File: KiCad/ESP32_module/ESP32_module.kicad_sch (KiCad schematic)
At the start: 35 parts, among them J1 Conn_01x05_Pin, J2 Conn_01x05_Pin, J3 Conn_01x05_Pin, J4 Conn_01x05_Pin, J5 Conn_01x02_Pin, J6 Conn_01x02_Pin, J7 Conn_01x02_Pin, J8 Conn_01x02_Pin, J9 Conn_01x02_Pin, M1 ESP32_XAIO

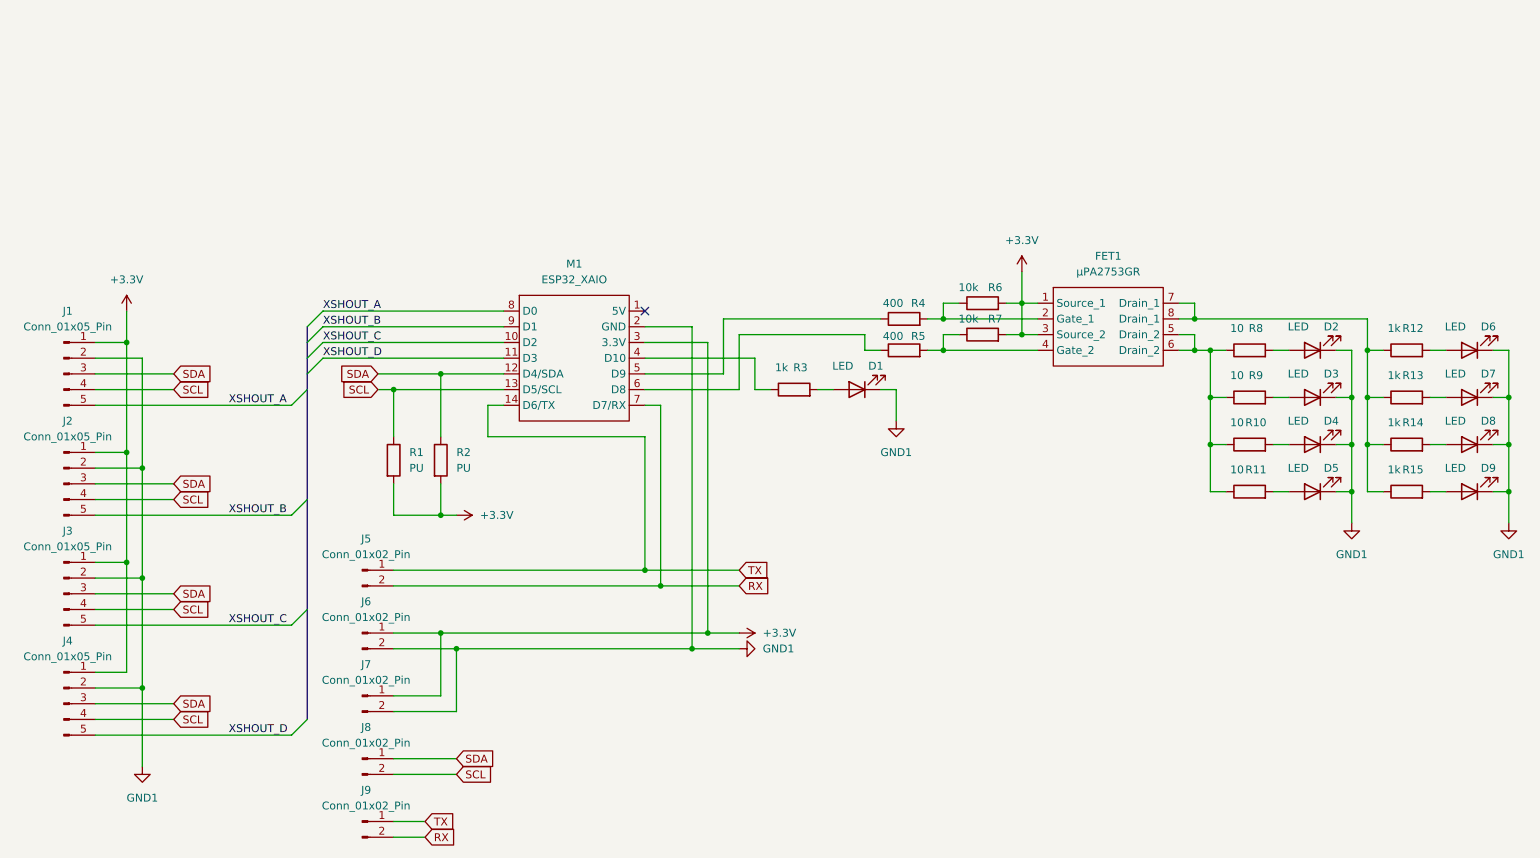
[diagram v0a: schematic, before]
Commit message: fix mosfet
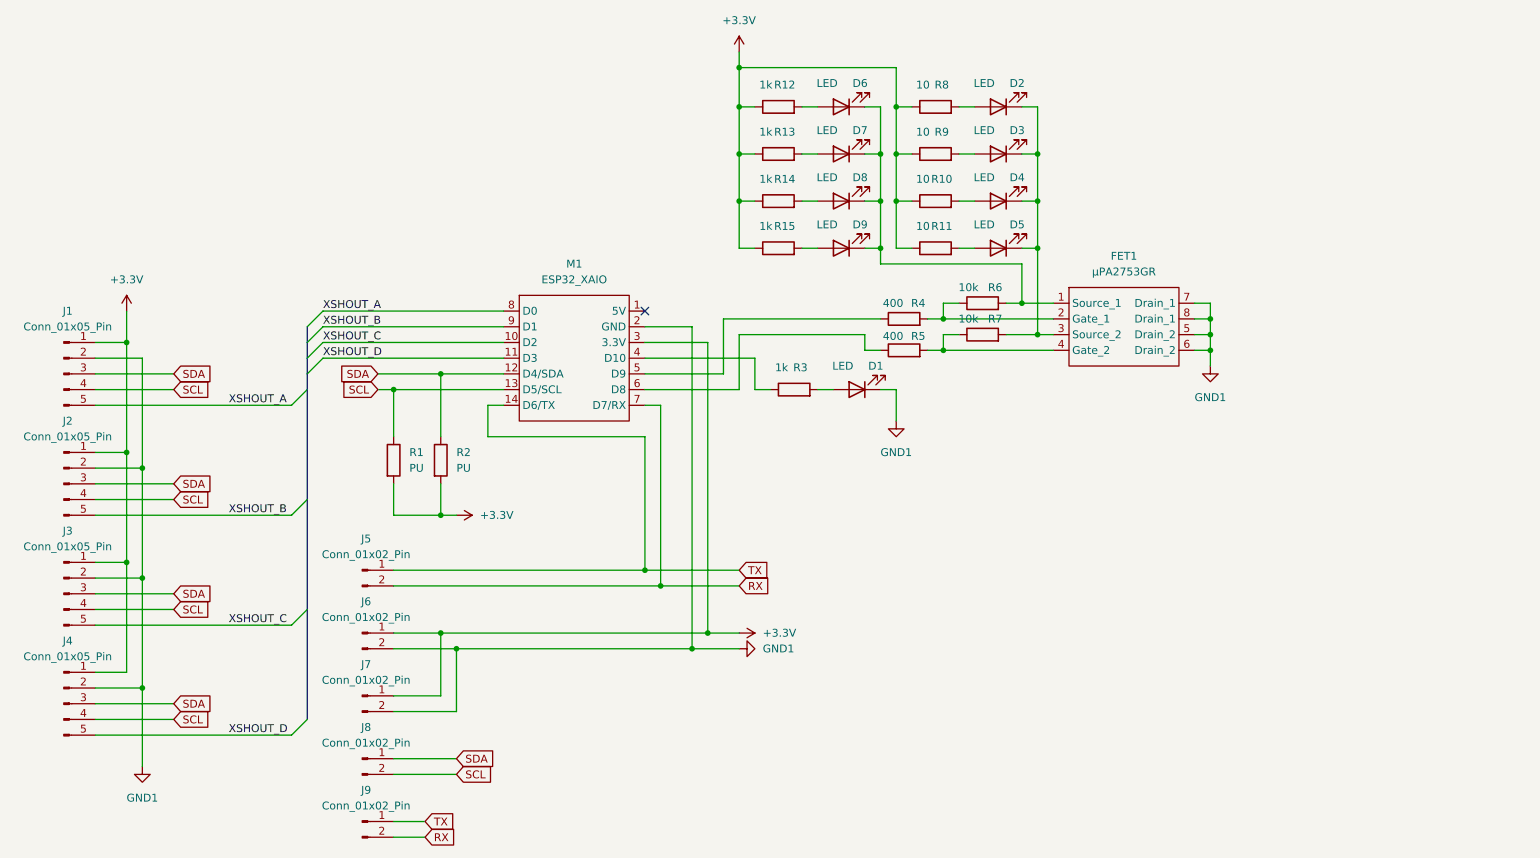
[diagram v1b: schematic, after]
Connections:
- net +3.3V: now also R10.1, R11.1, R12.1, R13.1, R14.1, R15.1, R8.1, R9.1; no longer FET1.1 (Source_1), FET1.3 (Source_2), R6.2, R7.2
- net GND1: now also FET1.5 (Drain_2), FET1.6 (Drain_2), FET1.7 (Drain_1), FET1.8 (Drain_1); no longer D2.1 (K), D3.1 (K), D4.1 (K), D5.1 (K), D6.1 (K), D7.1 (K), D8.1 (K), D9.1 (K)
- new net: D2.1 (K), D3.1 (K), D4.1 (K), D5.1 (K), FET1.3 (Source_2), R7.2
- new net: D6.1 (K), D7.1 (K), D8.1 (K), D9.1 (K), FET1.1 (Source_1), R6.2
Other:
- moved on the sheet: D2, D3, D4, D5, D6, D7, D8, D9, FET1, R10, R11, R12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

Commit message: fix
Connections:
- net GND1: now also FET1.1 (Source_1), FET1.3 (Source_2), R6.2, R7.2; no longer FET1.5 (Drain_2), FET1.6 (Drain_2), FET1.7 (Drain_1), FET1.8 (Drain_1)
- net at D2.1 (K), D3.1 (K), D4.1 (K)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: now also FET1.5 (Drain_2), FET1.6 (Drain_2); no longer FET1.3 (Source_2), R7.2
- net at D6.1 (K), D7.1 (K), D8.1 (K)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: now also FET1.7 (Drain_1), FET1.8 (Drain_1); no longer FET1.1 (Source_1), R6.2
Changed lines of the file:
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@@
 	)
 	(junction
-		(at 219.71 68.58)
-		(diameter 0)
-		(color 0 0 0 0)
-	)
-	(junction
-		(at 191.77 54.61)
-		(diameter 0)
-		(color 0 0 0 0)
-	)
-	(junction
 		(at 44.45 105.41)
 		(diameter 0)
@@
 	)
 	(junction
-		(at 191.77 68.58)
-		(diameter 0)
-		(color 0 0 0 0)
-	)
-	(junction
 		(at 130.81 109.22)
 		(diameter 0)
@@
 	)
 	(junction
+		(at 190.5 68.58)
+		(diameter 0)
+		(color 0 0 0 0)
+	)
+	(junction
 		(at 176.53 66.04)
 		(diameter 0)
@@
 	)
 	(junction
+		(at 219.71 63.5)
+		(diameter 0)
+		(color 0 0 0 0)
+	)
+	(junction
 		(at 166.37 39.37)
 		(diameter 0)
@@
 	)
 	(junction
-		(at 219.71 71.12)
+		(at 219.71 68.58)
 		(diameter 0)
 		(color 0 0 0 0)
 	)
 	(junction
-		(at 189.23 63.5)
+		(at 95.25 74.93)
 		(diameter 0)
 		(color 0 0 0 0)
 	)
 	(junction
-		(at 95.25 74.93)
+		(at 128.27 106.68)
 		(diameter 0)
 		(color 0 0 0 0)
 	)
 	(junction
-		(at 128.27 106.68)
+		(at 190.5 63.5)
+		(diameter 0)
+		(color 0 0 0 0)
+	)
+	(junction
+		(at 191.77 54.61)
 		(diameter 0)
 		(color 0 0 0 0)
@@
 	)
 	(junction
-		(at 219.71 66.04)
-		(diameter 0)
-		(color 0 0 0 0)
-	)
-	(junction
 		(at 46.99 125.73)
 		(diameter 0)
@@
 	(wire
 		(pts
+			(xy 190.5 63.5) (xy 190.5 68.58)
+		)
+		(stroke
+			(width 0)
+			(type default)
+		)
+	)
+	(wire
+		(pts
 			(xy 156.21 77.47) (xy 158.75 77.47)
 		)
@@
 	(wire
 		(pts
+			(xy 219.71 68.58) (xy 219.71 71.12)
+		)
+		(stroke
+			(width 0)
+			(type default)
+		)
+	)
+	(wire
+		(pts
+			(xy 190.5 68.58) (xy 190.5 76.2)
+		)
+		(stroke
+			(width 0)
+			(type default)
+		)
+	)
+	(wire
+		(pts
 			(xy 176.53 63.5) (xy 179.07 63.5)
 		)
@@
 	(wire
 		(pts
+			(xy 222.25 54.61) (xy 222.25 68.58)
+		)
+		(stroke
+			(width 0)
+			(type default)
+		)
+	)
+	(wire
+		(pts
 			(xy 168.91 46.99) (xy 171.45 46.99)
 		)
@@
 	(wire
 		(pts
+			(xy 219.71 68.58) (xy 222.25 68.58)
+		)
+		(stroke
+			(width 0)
+			(type default)
+		)
+	)
+	(wire
+		(pts
 			(xy 143.51 31.75) (xy 143.51 39.37)
 		)
@@
 	(wire
 		(pts
-			(xy 166.37 57.15) (xy 189.23 57.15)
+			(xy 219.71 57.15) (xy 219.71 63.5)
 		)
 		(stroke
@@
 	(wire
 		(pts
-			(xy 173.99 71.12) (xy 176.53 71.12)
+			(xy 191.77 54.61) (xy 222.25 54.61)
 		)
 		(stroke
@@
 	(wire
 		(pts
-			(xy 176.53 71.12) (xy 176.53 68.58)
+			(xy 166.37 57.15) (xy 219.71 57.15)
 		)
 		(stroke
@@
 	(wire
 		(pts
-			(xy 219.71 68.58) (xy 219.71 71.12)
+			(xy 173.99 71.12) (xy 176.53 71.12)
 		)
 		(stroke
@@
 	(wire
 		(pts
-			(xy 219.71 63.5) (xy 219.71 66.04)
+			(xy 176.53 71.12) (xy 176.53 68.58)
 		)
 		(stroke
@@
 	(wire
 		(pts
-			(xy 219.71 71.12) (xy 219.71 73.66)
-		)
-		(stroke
-			(width 0)
-			(type default)
-		)
-	)
-	(wire
-		(pts
 			(xy 168.91 25.4) (xy 168.91 31.75)
 		)
@@
 		)
 	)
-	(bus
-		(pts
-			(xy 73.66 72.39) (xy 73.66 74.93)
-		)
-		(stroke
-			(width 0)
-			(type default)
-		)
-	)
 	(wire
 		(pts
-			(xy 186.69 63.5) (xy 189.23 63.5)
+			(xy 190.5 68.58) (xy 194.31 68.58)
 		)
 		(stroke
@@
 		)
 	)
-	(wire
+	(bus
 		(pts
-			(xy 143.51 46.99) (xy 146.05 46.99)
+			(xy 73.66 72.39) (xy 73.66 74.93)
 		)
 		(stroke
@@
 	(wire
 		(pts
-			(xy 191.77 68.58) (xy 194.31 68.58)
+			(xy 143.51 46.99) (xy 146.05 46.99)
 		)
 		(stroke
@@
 	(wire
 		(pts
-			(xy 44.45 69.85) (xy 44.45 87.63)
+			(xy 190.5 63.5) (xy 194.31 63.5)
 		)
 		(stroke
@@
 	(wire
 		(pts
-			(xy 76.2 64.77) (xy 105.41 64.77)
+			(xy 44.45 69.85) (xy 44.45 87.63)
 		)
 		(stroke
@@
 	(wire
 		(pts
-			(xy 138.43 69.85) (xy 138.43 116.84)
+			(xy 76.2 64.77) (xy 105.41 64.77)
 		)
 		(stroke
@@
 	(wire
 		(pts
-			(xy 189.23 57.15) (xy 189.23 63.5)
+			(xy 138.43 69.85) (xy 138.43 116.84)
 		)
 		(stroke
@@
 	(wire
 		(pts
+			(xy 219.71 63.5) (xy 219.71 66.04)
+		)
+		(stroke
+			(width 0)
+			(type default)
+		)
+	)
+	(wire
+		(pts
 			(xy 217.17 68.58) (xy 219.71 68.58)
 		)
@@
 	(wire
 		(pts
-			(xy 219.71 66.04) (xy 219.71 68.58)
-		)
-		(stroke
-			(width 0)
-			(type default)
-		)
-	)
-	(wire
-		(pts
 			(xy 46.99 72.39) (xy 46.99 90.17)
 		)
@@
 	(wire
 		(pts
-			(xy 189.23 63.5) (xy 194.31 63.5)
+			(xy 186.69 63.5) (xy 190.5 63.5)
 		)
 		(stroke
@@
 	(wire
 		(pts
-			(xy 191.77 54.61) (xy 191.77 68.58)
-		)
-		(stroke
-			(width 0)
-			(type default)
-		)
-	)
-	(wire
-		(pts
 			(xy 87.63 119.38) (xy 97.79 119.38)
 		)
@@
 	(wire
 		(pts
-			(xy 186.69 68.58) (xy 191.77 68.58)
+			(xy 186.69 68.58) (xy 190.5 68.58)
 		)
 		(stroke
@@
 	(symbol
 		(lib_id "power:GND1")
-		(at 219.71 73.66 0)
+		(at 190.5 76.2 0)
 		(unit 1)
 		(exclude_from_sim no)
@@
 		(fields_autoplaced yes)
 		(property "Reference" "#PWR09"
-			(at 219.71 80.01 0)
+			(at 190.5 82.55 0)
 			(effects
 				(font
@@
 		)
 		(property "Value" "GND1"
-			(at 219.71 78.74 0)
+			(at 190.5 81.28 0)
 			(effects
 				(font
@@
 		)
 		(property "Footprint" ""
-			(at 219.71 73.66 0)
+			(at 190.5 76.2 0)
 			(effects
 				(font
@@
 		)
 		(property "Datasheet" ""
-			(at 219.71 73.66 0)
+			(at 190.5 76.2 0)
 			(effects
 				(font
@@
 		)
 		(property "Description" "Power symbol creates a global label with name \"GND1\" , ground"
-			(at 219.71 73.66 0)
+			(at 190.5 76.2 0)
 			(effects
 				(font
